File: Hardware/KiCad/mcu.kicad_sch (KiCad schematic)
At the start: 12 parts, among them U3 STM32F427ZGTx, Y1 8 MHz, Y2 32 kHz

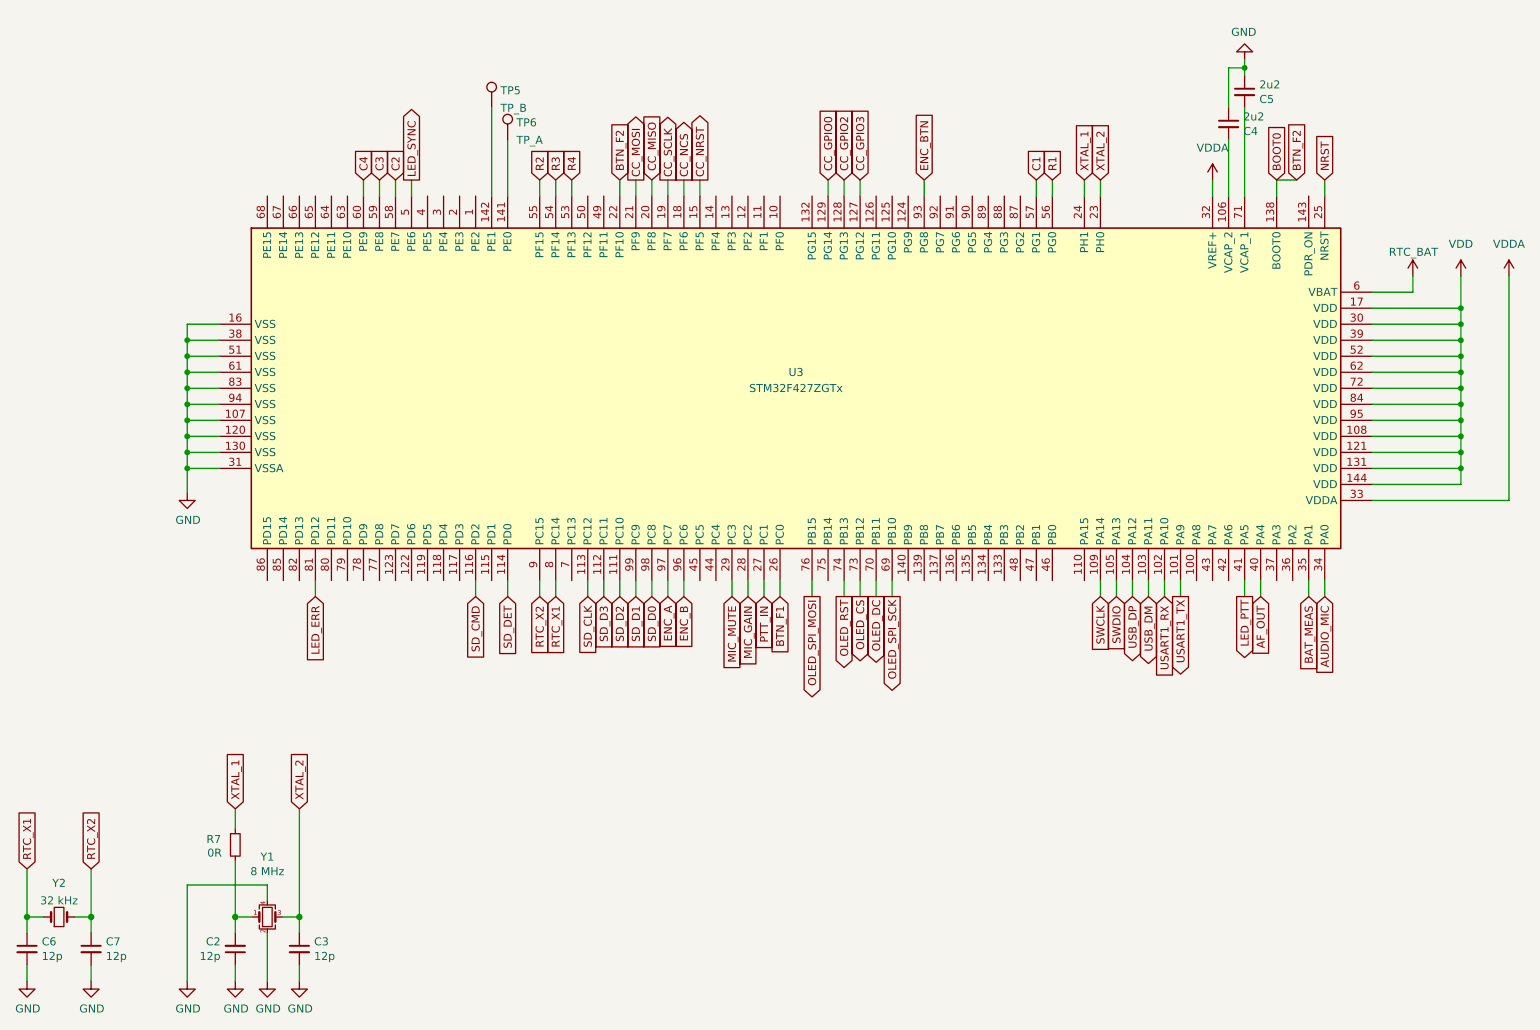
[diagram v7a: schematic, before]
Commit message: many edits throughout, added board edges for main & HMI combined, added rough layouts for some components on both
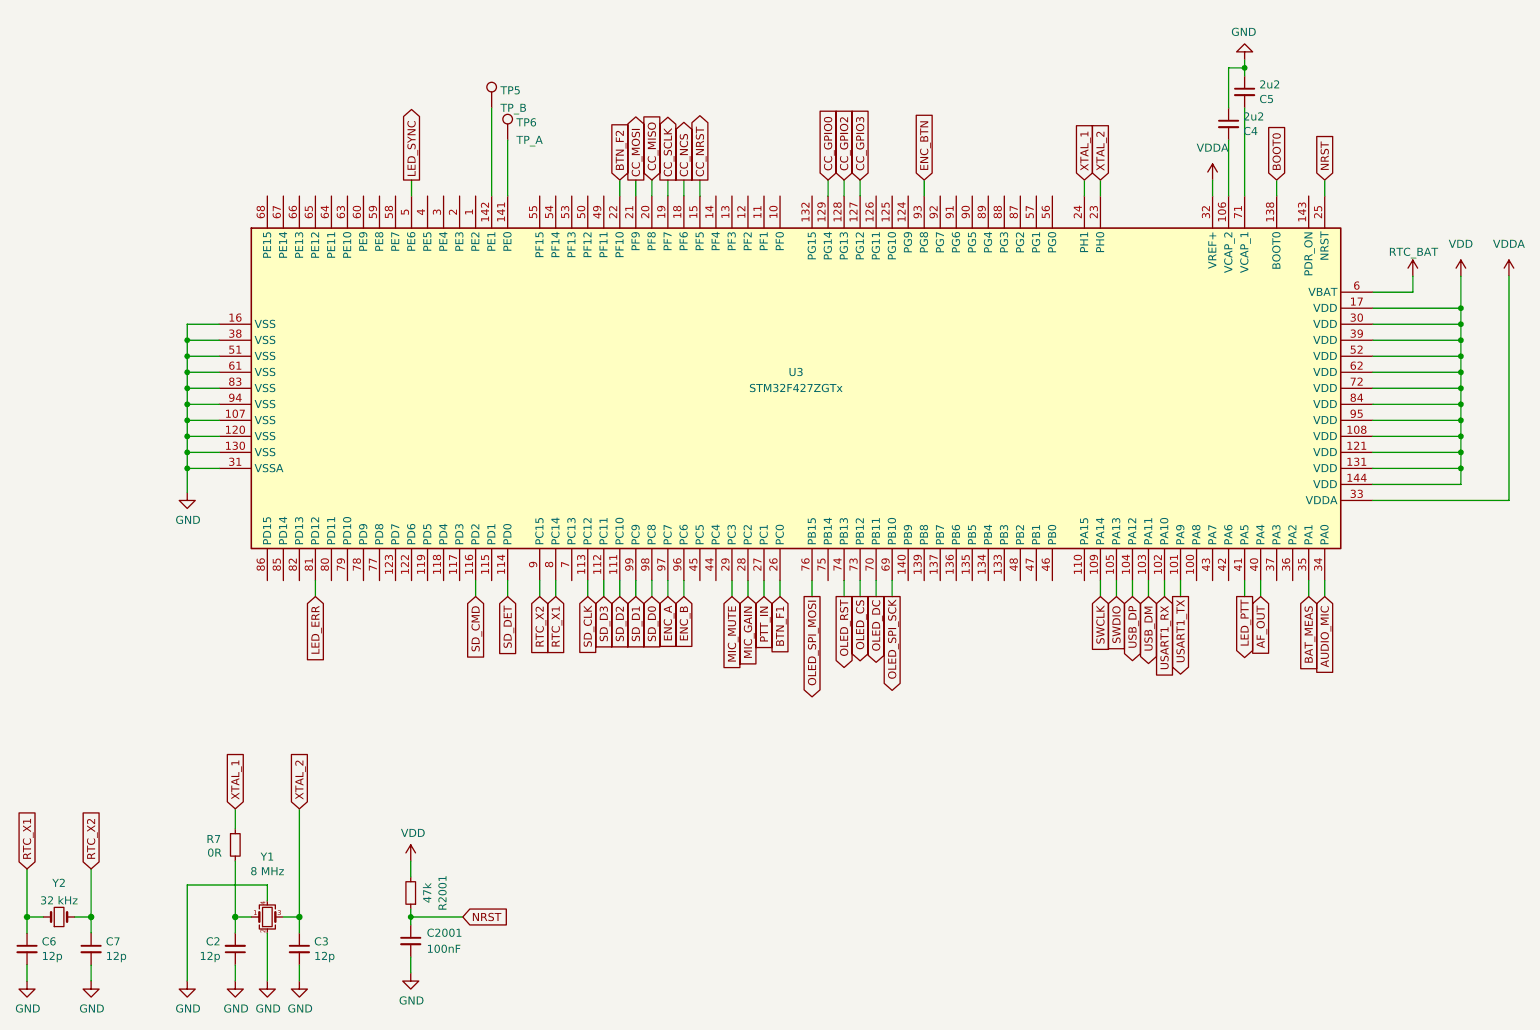
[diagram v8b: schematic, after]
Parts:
- added C2001: 100nF, Capacitor_SMD:C_0402_1005Metric, symbol Device:C_Small
- added R2001: 47k, Resistor_SMD:R_0402_1005Metric, symbol pkl_device:pkl_R_Small
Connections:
- net BOOT0: no longer U3.22 (PF10)
- net GND: now also C2001.2
- net NRST: now also C2001.1, R2001.1
- net VDD: now also R2001.2
- net C1: no longer names the net of U3.57 (PG1)
- net C2: no longer names the net of U3.58 (PE7)
- net C3: no longer names the net of U3.59 (PE8)
- net C4: no longer names the net of U3.60 (PE9)
- net R1: no longer names the net of U3.56 (PG0)
- net R2: no longer names the net of U3.55 (PF15)
- net R3: no longer names the net of U3.54 (PF14)
- net R4: no longer names the net of U3.53 (PF13)
- new net BTN_F2: U3.22 (PF10)
